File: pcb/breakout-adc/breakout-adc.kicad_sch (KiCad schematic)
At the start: 26 parts, among them J1 Screw_Terminal_01x04, J10 Conn_01x01_Pin, J11 Conn_01x12_Pin, J12 Conn_01x12_Pin, J13 Conn_01x01_Pin, J14 Conn_01x01_Pin, J15 FX18-120P-0.8SV20, J16 Conn_01x01_Pin, J17 Conn_01x01_Pin, J18 Conn_01x01_Pin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

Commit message: [adc][pcb] clear adc simulator flag
also start adding part numbers
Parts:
- C40, C41, C42: Digi-Key Part Number (none) -> 490-GRT1555C1H161FA02DCT-ND; LCSC Part # (none) -> C2188753
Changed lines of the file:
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@@
+			)
+		)
+		(property "Digi-Key Part Number" "490-GRT1555C1H161FA02DCT-ND"
+			(at 181.61 144.78 0)
+			(effects
+				(font
+					(size 1.27 1.27)
+				)
+				(hide yes)
+			)
+		)
+		(property "LCSC Part #" "C2188753"
+			(at 181.61 144.78 0)
+			(effects
+				(font
+					(size 1.27 1.27)
+				)
+				(hide yes)
 			)
 		)
@@
 			)
 		)
+		(property "Digi-Key Part Number" "490-GRT1555C1H161FA02DCT-ND"
+			(at 170.18 144.78 0)
+			(effects
+				(font
+					(size 1.27 1.27)
+				)
+				(hide yes)
+			)
+		)
+		(property "LCSC Part #" "C2188753"
+			(at 170.18 144.78 0)
+			(effects
+				(font
+					(size 1.27 1.27)
+				)
+				(hide yes)
+			)
+		)
 		(pin "1"
 		)
@@
 			(at 158.75 144.78 0)
 			(effects
+				(font
+					(size 1.27 1.27)
+				)
+				(hide yes)
+			)
+		)
+		(property "Digi-Key Part Number" "490-GRT1555C1H161FA02DCT-ND"
+			(at 158.75 144.78 0)
+			(effects
+				(font
+					(size 1.27 1.27)
+				)
+				(hide yes)
+			)
+		)
+		(property "LCSC Part #" "C2188753"
+			(at 158.75 144.78 0)
+			(effects

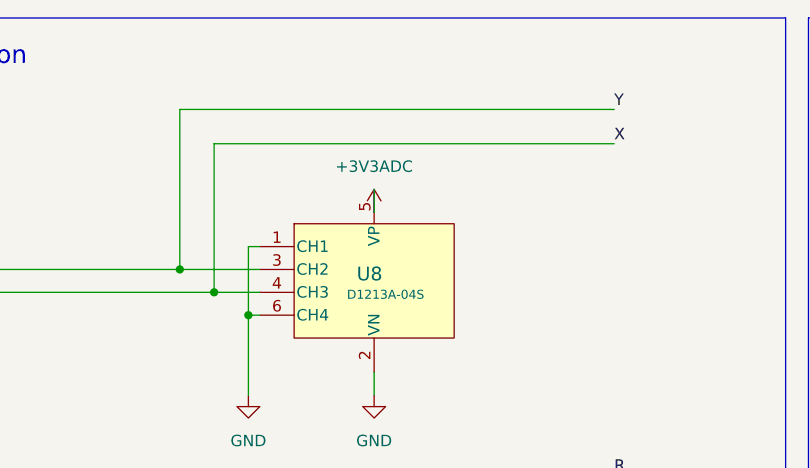
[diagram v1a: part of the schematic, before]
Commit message: [adc][pcb] add remaining part numbers
missing test points for lcsc, but otherwise done
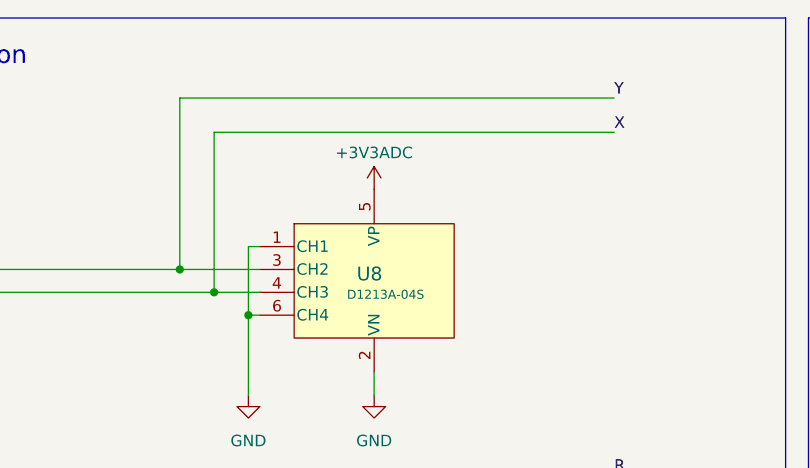
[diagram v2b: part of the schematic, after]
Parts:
- J1: Digi-Key Part Number (none) -> 277-1208-ND; LCSC Part # (none) -> C480536
- J10, J14, J16, J17, J18, J5, J6: value Conn_01x01_Pin -> Black; Digi-Key Part Number (none) -> 36-5001-ND
- J11, J12: value Conn_01x12_Pin -> Conn_02x06_Pin; Digi-Key Part Number (none) -> 952-2125-ND
- J13, J7: value Conn_01x01_Pin -> Red; Digi-Key Part Number (none) -> 36-5000-ND
- J2: value Screw_Terminal_01x02 -> Screw_Terminal_01x06; Digi-Key Part Number (none) -> 277-1210-ND; LCSC Part # (none) -> C480580
- J3, J4: value Conn_01x01_Pin -> White; Digi-Key Part Number (none) -> 36-5002-ND
- J8: value Conn_01x01_Pin -> Green; Digi-Key Part Number (none) -> 36-5116-ND
- J9: value Conn_01x01_Pin -> Blue; Digi-Key Part Number (none) -> 36-5117-ND
- R1, R2, R3: Digi-Key Part Number (none) -> 311-523HRCT-ND; LCSC Part # (none) -> C227952
- U8, U9: Digi-Key Part Number (none) -> D1213A:SOT-363_DIO; LCSC Part # (none) -> C460587

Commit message: [adc][pcb] fix digikey part for ESD protection
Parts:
- U8: Digi-Key Part Number D1213A:SOT-363_DIO -> D1213A-04S-7DICT-ND
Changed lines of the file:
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@@
 			)
 		)
-		(property "Digi-Key Part Number" "D1213A:SOT-363_DIO "
+		(property "Digi-Key Part Number" "D1213A-04S-7DICT-ND"
 			(at 111.76 46.99 0)
 			(effects

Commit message: [adc][pcb] add esd datasheet
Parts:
- U8, U9: footprint D1213A:SOT-363_DIO -> SOT-363_DIO
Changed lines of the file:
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@@
 	)
 	(symbol
+		(lib_name "D1213A-04S-7_1")
 		(lib_id "D1213A-04S:D1213A-04S-7")
 		(at 111.76 46.99 0)
@@
 			)
 		)
-		(property "Footprint" "D1213A:SOT-363_DIO"
+		(property "Footprint" "SOT-363_DIO"
 			(at 111.76 46.99 0)
 			(effects
@@
 			)
 		)
-		(property "Datasheet" "D1213A-04S-7"
+		(property "Datasheet" "https://www.diodes.com/assets/Datasheets/D1213A-04S.pdf"
 			(at 111.76 46.99 0)
 			(effects
@@
 			)
 		)
-		(property "Footprint" "D1213A:SOT-363_DIO"
+		(property "Footprint" "SOT-363_DIO"
 			(at 111.76 97.79 0)
 			(effects
@@
 			)
 		)
-		(property "Datasheet" "D1213A-04S-7"
+		(property "Datasheet" "https://www.diodes.com/assets/Datasheets/D1213A-04S.pdf"
 			(at 111.76 97.79 0)
 			(effects

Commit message: [adc][pcb] fabtoolkit config
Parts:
- U9: Digi-Key Part Number D1213A:SOT-363_DIO -> D1213A-04S-7DICT-ND
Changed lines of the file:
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@@
 			)
 		)
-		(property "Digi-Key Part Number" "D1213A:SOT-363_DIO "
+		(property "Digi-Key Part Number" "D1213A-04S-7DICT-ND"
 			(at 111.76 97.79 0)
 			(effects

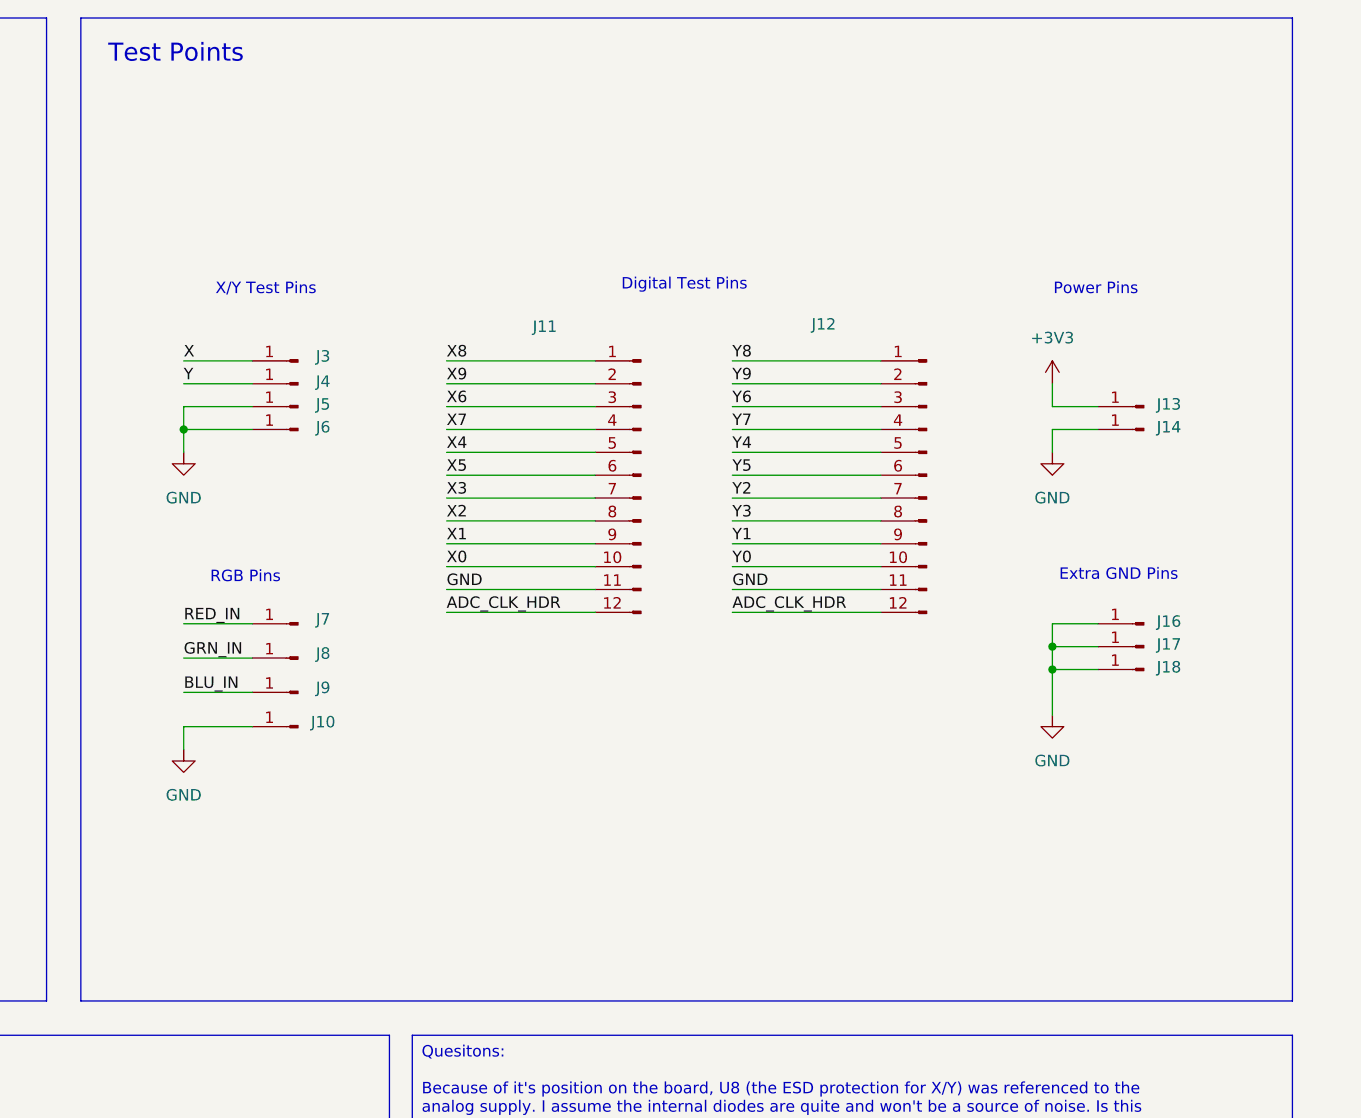
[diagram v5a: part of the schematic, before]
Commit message: [adc][pcb] add x/y vcm test points
also fixed some drc issues that somehow snuck in,
specifically, the esd diodes weren't correctly linked
to their footprint, despite the footprint being physically
correct on the pcb
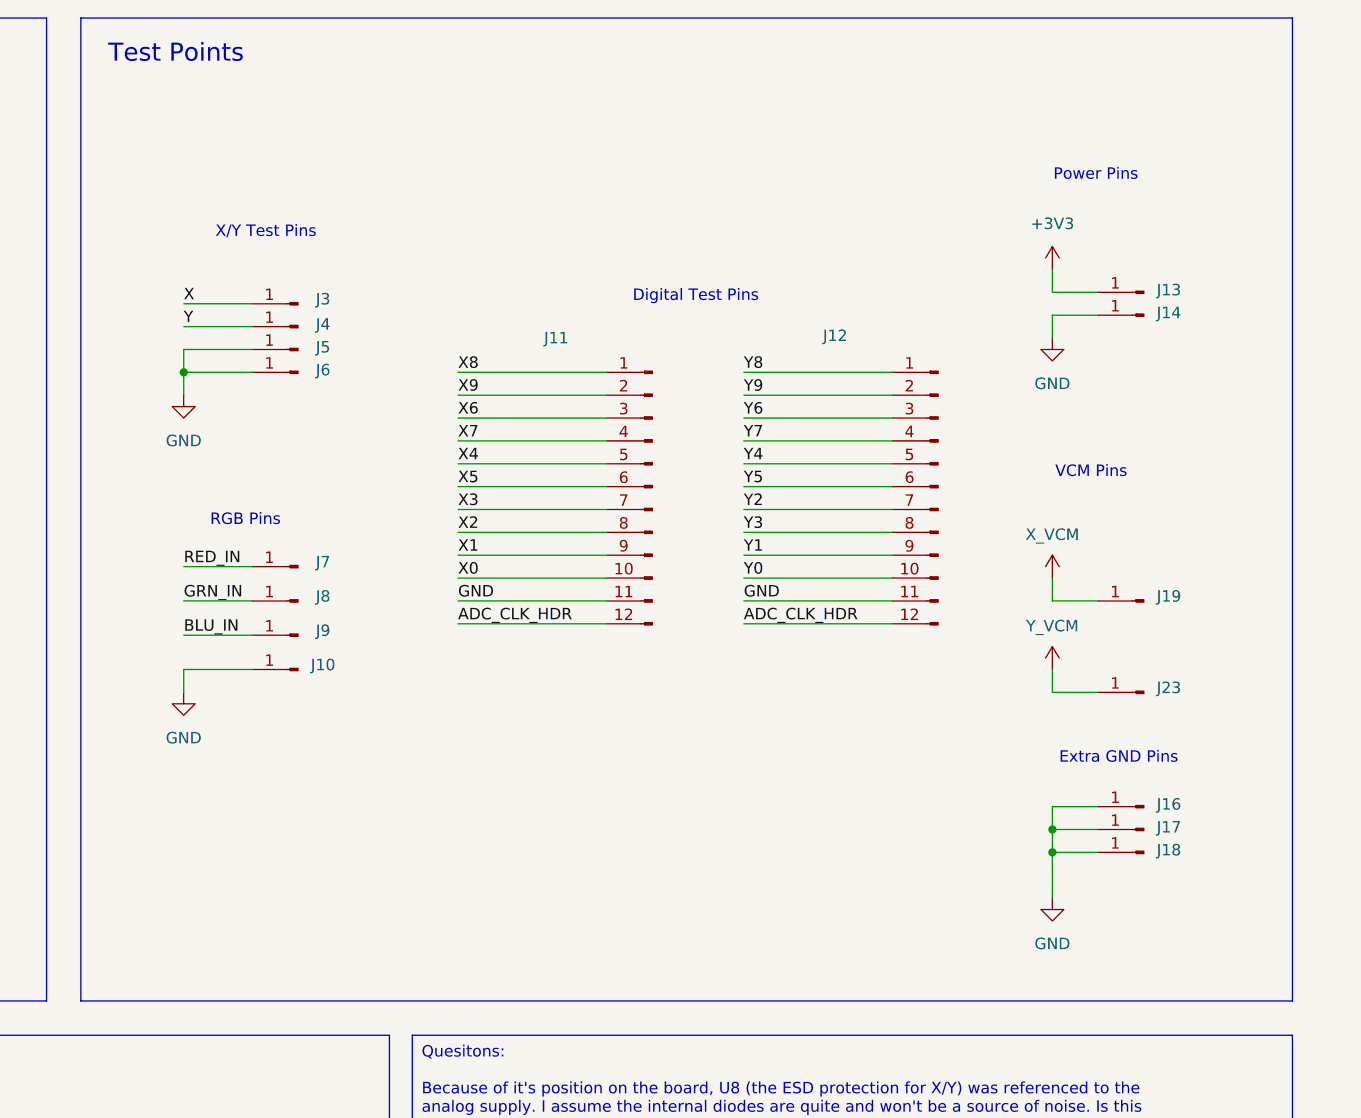
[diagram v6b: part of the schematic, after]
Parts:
- added J19, J23: Blue, keystone:KEYSTONE_5117, symbol Connector:Conn_01x01_Pin
- U8, U9: footprint SOT-363_DIO -> D1213A:SOT-363_DIO
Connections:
- new net X_VCM: J19.1 (Pin_1)
- new net Y_VCM: J23.1 (Pin_1)
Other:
- note added: "VCM Pins"
- moved on the sheet: J10, J11, J12, J13, J14, J16, J17, J18, J3, J4, J5, J6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

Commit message: [adc][pcb] fix output buffer schematic and routing
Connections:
- net X4: now also J11.6 (Pin_6), J15.67; no longer J11.5 (Pin_5), J15.68
- net X5: now also J11.5 (Pin_5), J15.68; no longer J11.6 (Pin_6), J15.67
- net Y2: now also J12.8 (Pin_8), J15.78; no longer J12.7 (Pin_7), J15.77
- net Y3: now also J12.7 (Pin_7), J15.77; no longer J12.8 (Pin_8), J15.78
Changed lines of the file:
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@@
 	)
 	(label "Y3"
-		(at 146.05 187.96 180)
+		(at 146.05 190.5 180)
 		(fields_autoplaced yes)
 		(effects
@@
 	)
 	(label "Y3"
-		(at 347.98 74.93 0)
+		(at 347.98 72.39 0)
 		(fields_autoplaced yes)
 		(effects
@@
 	)
 	(label "X5"
-		(at 316.23 69.85 0)
+		(at 316.23 67.31 0)
 		(fields_autoplaced yes)
 		(effects
@@
 	)
 	(label "Y2"
-		(at 146.05 190.5 180)
+		(at 146.05 187.96 180)
 		(fields_autoplaced yes)
 		(effects
@@
 	)
 	(label "X4"
-		(at 146.05 213.36 180)
+		(at 146.05 215.9 180)
 		(fields_autoplaced yes)
 		(effects
@@
 	)
 	(label "X4"
-		(at 316.23 67.31 0)
+		(at 316.23 69.85 0)
 		(fields_autoplaced yes)
 		(effects
@@
 	)
 	(label "Y2"
-		(at 347.98 72.39 0)
+		(at 347.98 74.93 0)
 		(fields_autoplaced yes)
 		(effects
@@
 	)
 	(label "X5"
-		(at 146.05 215.9 180)
-		(fields_autoplaced yes)
-		(effects
+		(at 146.05 213.36 180)
+		(fields_autoplaced yes)
+		(effects

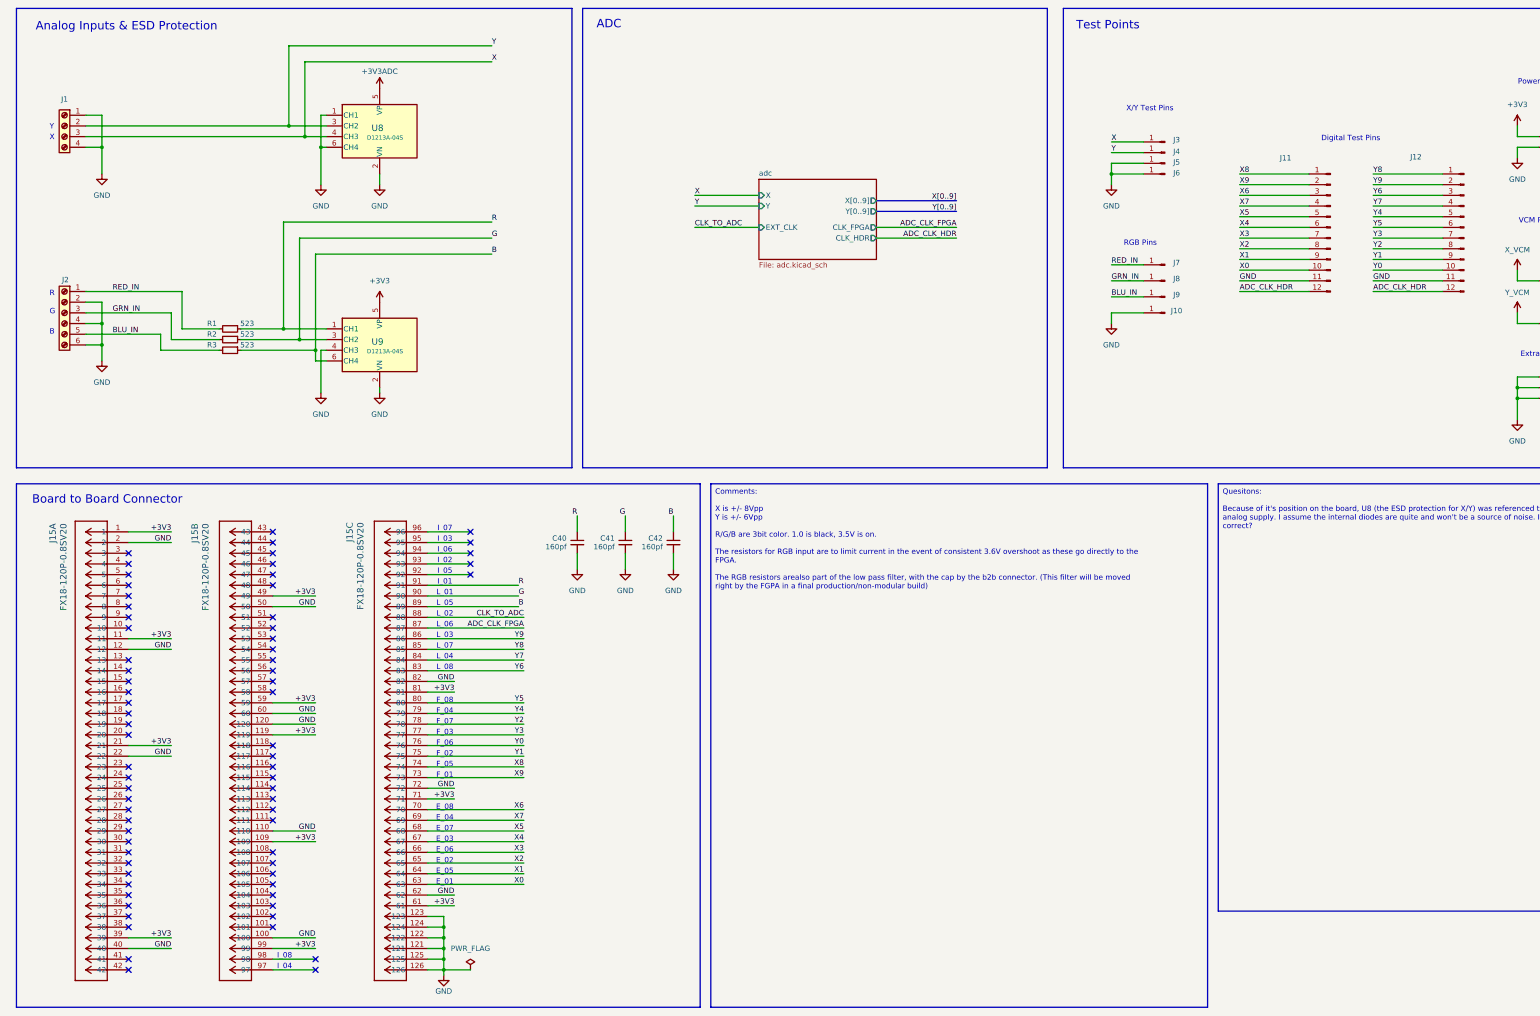
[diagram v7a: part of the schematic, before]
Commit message: [adc][pcb] stackable version
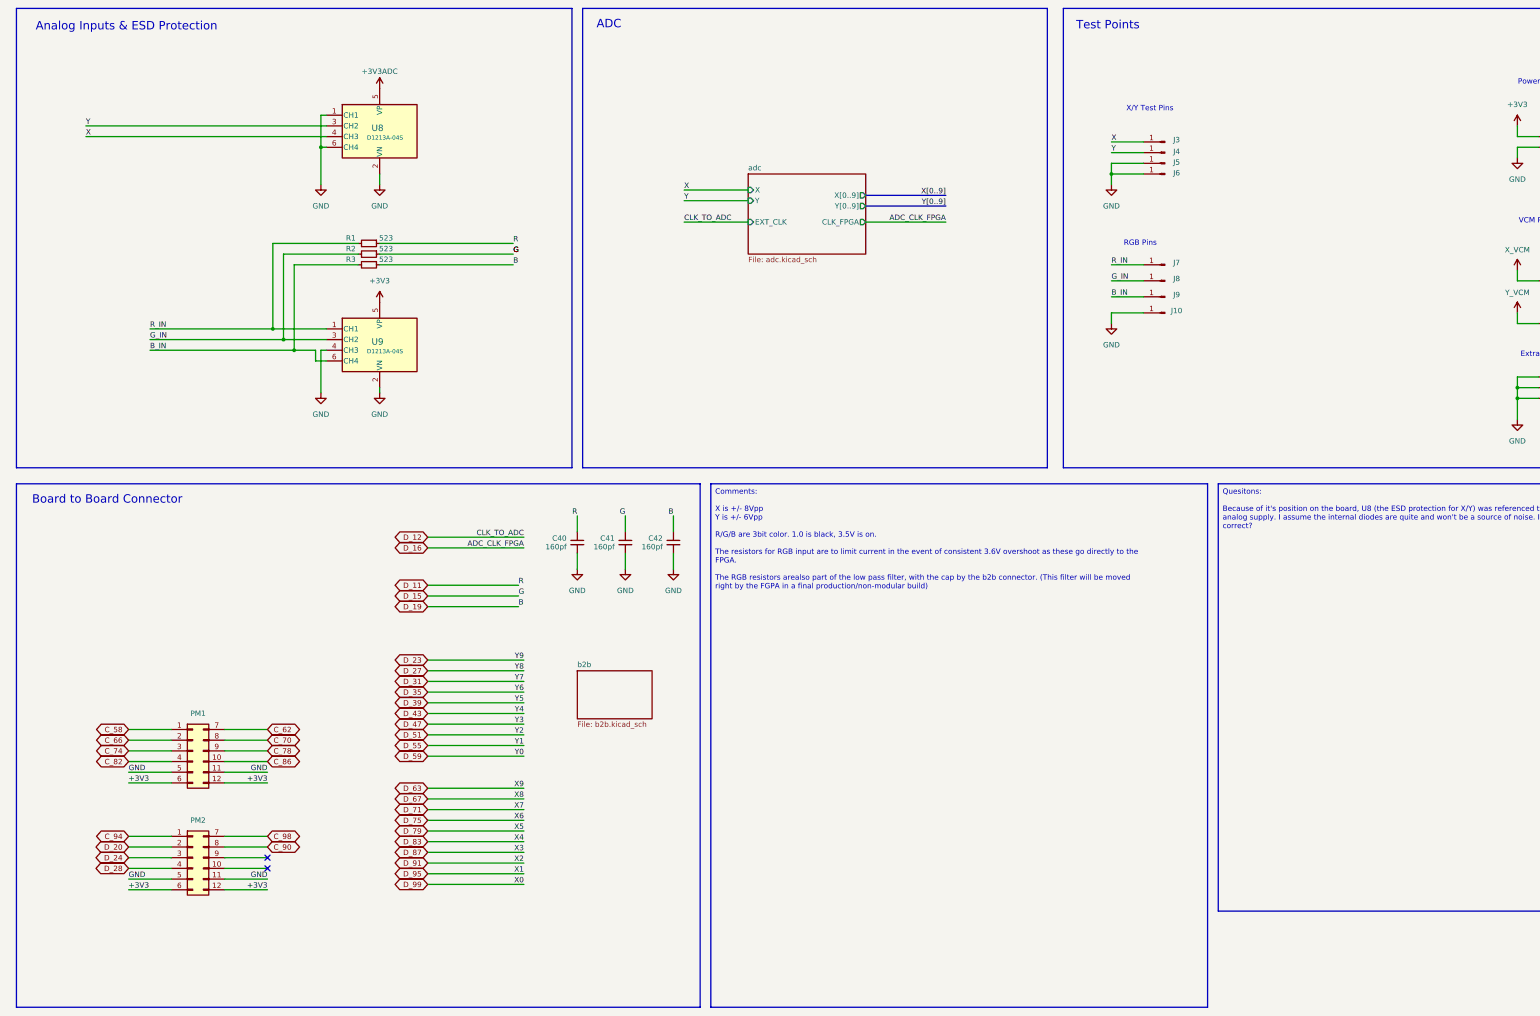
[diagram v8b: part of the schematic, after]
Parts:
- removed J1: Screw_Terminal_01x04, Connector_Phoenix_MC:PhoenixContact_MC_1,5_4-G-3.81_1x04_P3.81mm_Horizontal, symbol Connector:Screw_Terminal_01x04
- removed J11, J12: Conn_02x06_Pin, Connector_PinHeader_2.54mm:PinHeader_2x06_P2.54mm_Vertical, symbol Connector:Conn_01x12_Pin
- removed J15: FX18-120P-0.8SV20, custom:CUSTOM_FX_120P-0.8SH20, symbol FX18-120P-0-8SV20:FX18-120P-0.8SV20
- removed J2: Screw_Terminal_01x06, Connector_Phoenix_MC:PhoenixContact_MC_1,5_6-G-3.81_1x06_P3.81mm_Horizontal, symbol Connector:Screw_Terminal_01x06
- added PM1, PM2: Conn_02x06_Top_Bottom, custom:PMOD_12p_Horizontal, symbol Connector_Generic:Conn_02x06_Top_Bottom
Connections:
- net +3V3: now also PM1.12 (Pin_12), PM1.6 (Pin_6), PM2.12 (Pin_12), PM2.6 (Pin_6)
- net GND: now also PM1.11 (Pin_11), PM1.5 (Pin_5), PM2.11 (Pin_11), PM2.5 (Pin_5)
- net B renamed D_19
- net D_19: no longer U9.6 (CH4)
- net BLU_IN renamed B_IN
- net B_IN: now also U9.6 (CH4)
- net G renamed D_15
- net D_15: no longer U9.3 (CH2)
- net GRN_IN renamed G_IN
- net G_IN: now also U9.3 (CH2)
- net R renamed D_11
- net D_11: no longer U9.1 (CH1)
- net RED_IN renamed R_IN
- net R_IN: now also U9.1 (CH1)
- new net C_58: PM1.1 (Pin_1)
- new net C_62: PM1.7 (Pin_7)
- new net C_66: PM1.2 (Pin_2)
- new net C_70: PM1.8 (Pin_8)
- new net C_74: PM1.3 (Pin_3)
- new net C_78: PM1.9 (Pin_9)
- new net C_82: PM1.4 (Pin_4)
- new net C_86: PM1.10 (Pin_10)
- new net C_90: PM2.8 (Pin_8)
- new net C_94: PM2.1 (Pin_1)
- new net C_98: PM2.7 (Pin_7)
- new net D_20: PM2.2 (Pin_2)
- new net D_24: PM2.3 (Pin_3)
- new net D_28: PM2.4 (Pin_4)
- no-connect marks 71 -> 2
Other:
- added sheet b2b (b2b.kicad_sch)
- sheet adc ports: added none; removed CLK_HDR
- note removed: "B"
- note removed: "Digital Test Pins"
- note removed: "E_01"
- note removed: "E_02"
- note removed: "E_03"
- note removed: "E_04"
- note removed: "E_05"
- note removed: "E_06"
- note removed: "E_07"
- note removed: "E_08"
- note removed: "F_01"
- note removed: "F_02"
- note removed: "F_03"
- note removed: "F_04"
- note removed: "F_05"
- note removed: "F_06"
- note removed: "F_07"
- note removed: "F_08"
- note removed: "G"
- note removed: "I_01"
- note removed: "I_02"
- note removed: "I_03"
- note removed: "I_04"
- note removed: "I_05"
- note removed: "I_06"
- note removed: "I_07"
- note removed: "I_08"
- note removed: "L_01"
- note removed: "L_02"
- note removed: "L_03"
- note removed: "L_04"
- note removed: "L_05"
- note removed: "L_06"
- note removed: "L_07"
- note removed: "L_08"
- note removed: "R"
- note removed: "X"
- note removed: "Y"
- moved on the sheet: R1, R2, R3
